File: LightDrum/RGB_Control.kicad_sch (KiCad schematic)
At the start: 0 parts

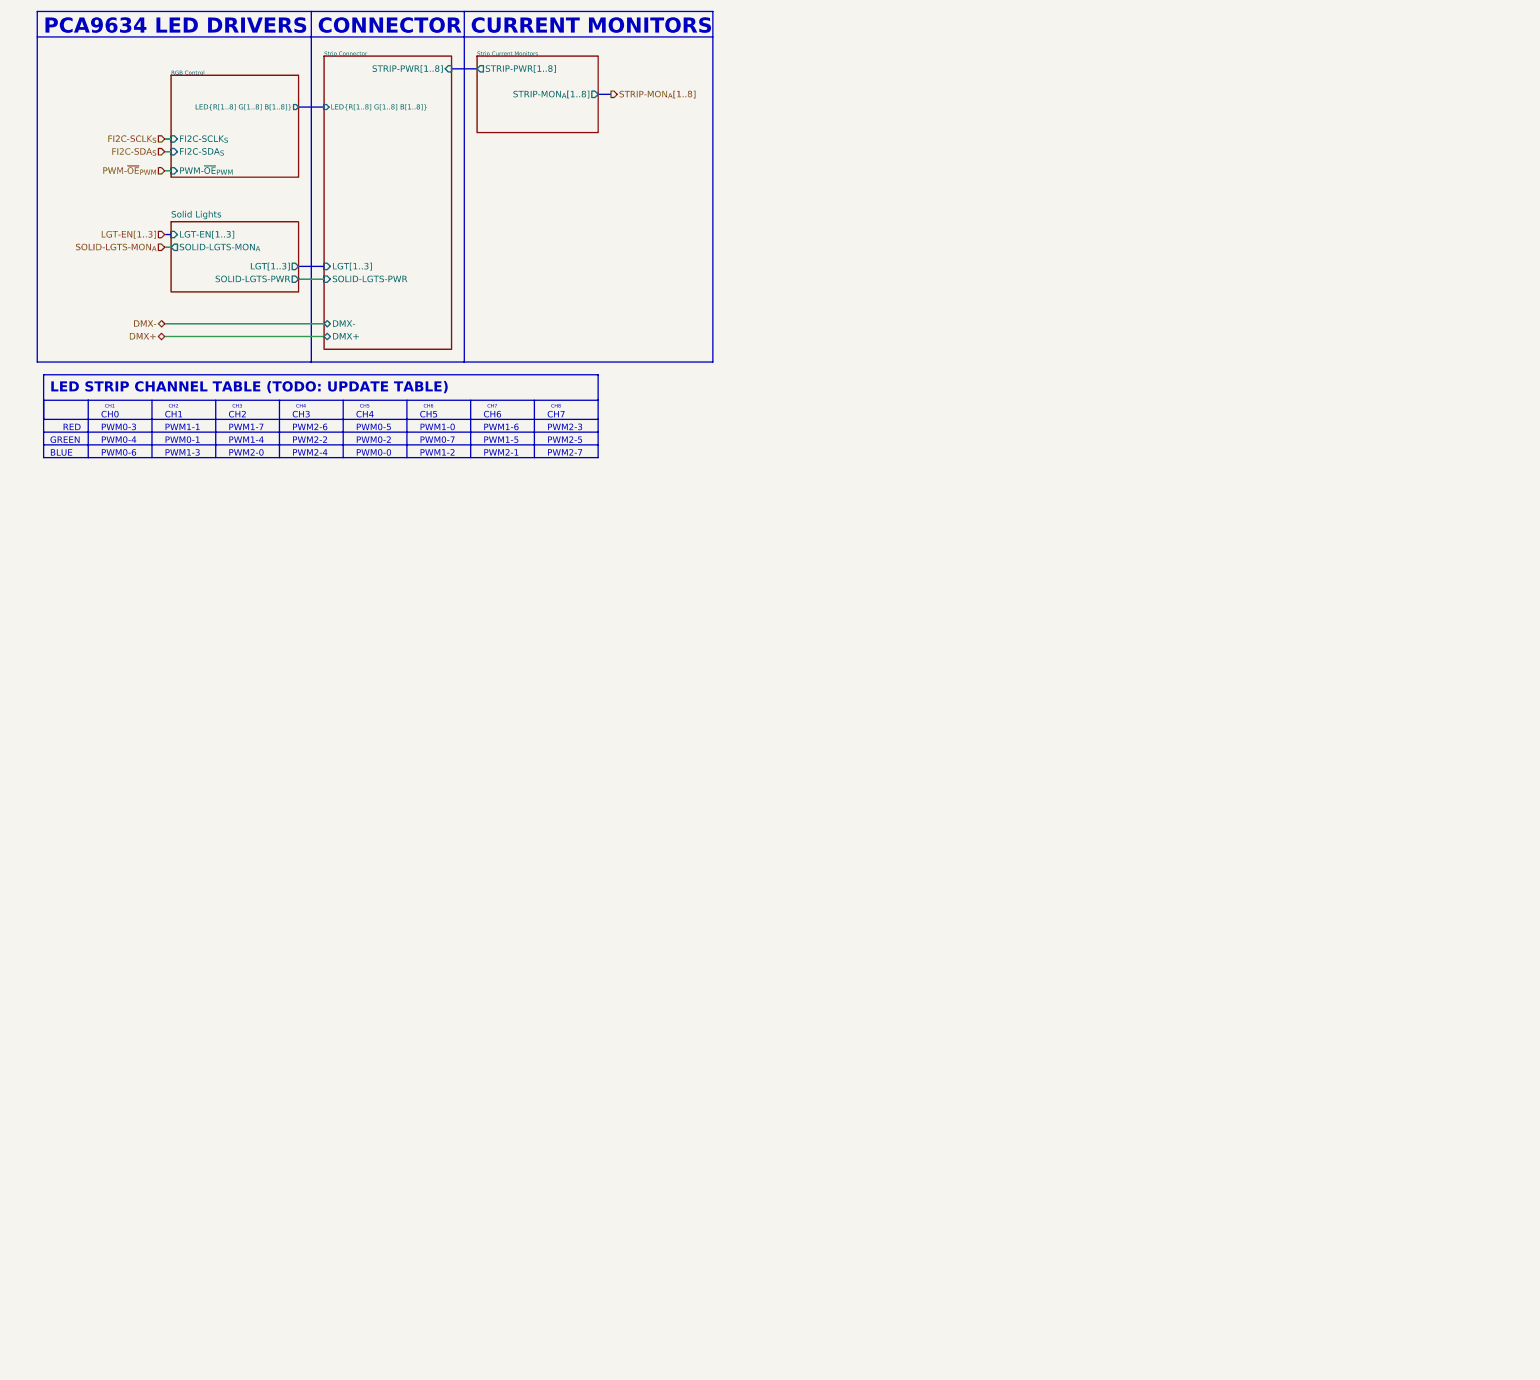
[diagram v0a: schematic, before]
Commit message: Fix schematic layout
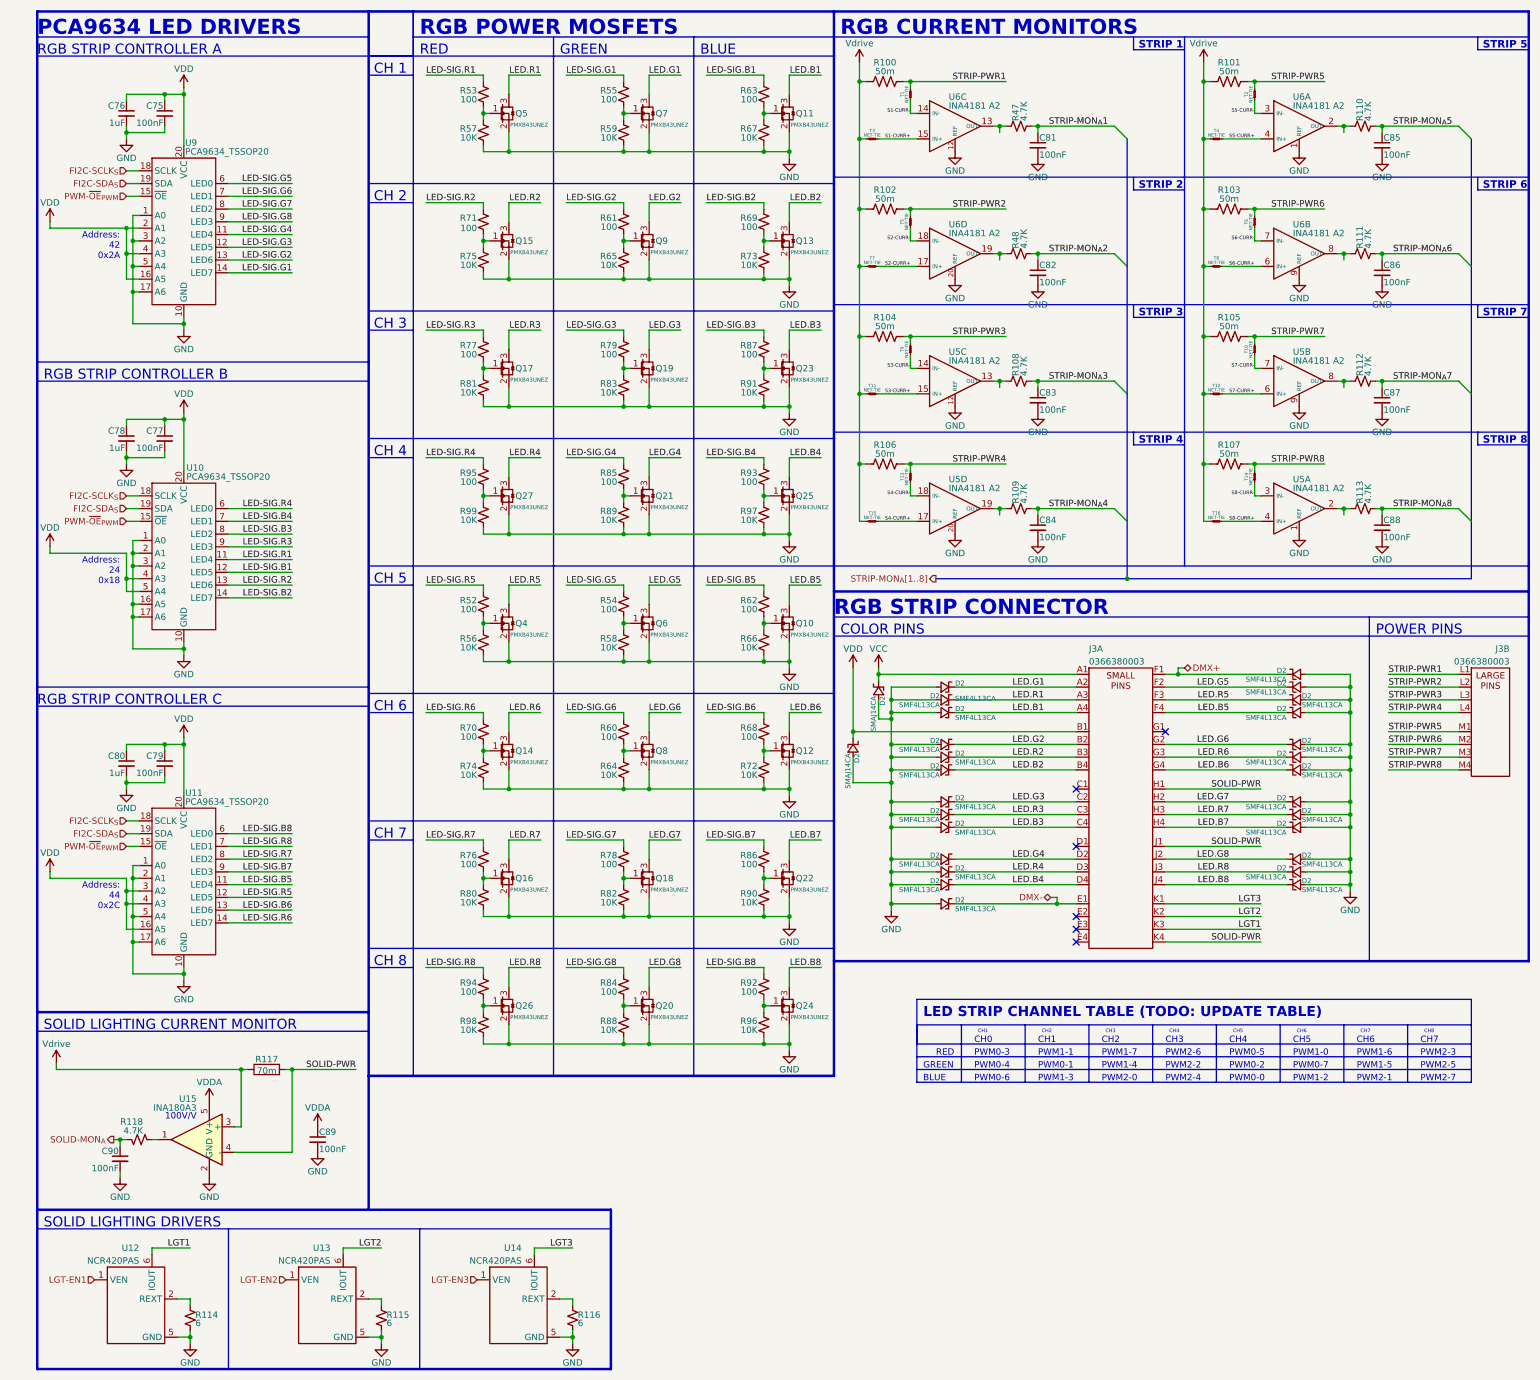
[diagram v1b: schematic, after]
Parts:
- added C75, C77, C79, C81, C82, C83, C84, C85, C86, C87, C88, C89, C90: 100nF, Capacitor_SMD:C_0402_1005Metric, symbol Daxxn_Device:C
- added C76, C78, C80: 1uF, Capacitor_SMD:C_0603_1608Metric, symbol Daxxn_Device:C
- added D2 (x26): SMF4L13CA, Diode_SMD:D_SOD-123F, symbol Daxxn_Device:D_TVS_U
- added D2 (x2): SMAJ14CA, Diode_SMD:D_SMA, symbol Daxxn_Device:D_TVS_U
- added J3: 0366380003, Daxxn_Connectors:0366380003, symbol Daxxn_Connectors:0366380003
- added Q10, Q11, Q12, Q13, Q14, Q15, Q16, Q17, Q18, Q19, Q20, Q21, Q22, Q23, Q24, Q25, Q26, Q27, Q4, Q5, Q6, Q7, Q8, Q9: PMXB43UNEZ, Daxxn_Packages:DFN1010D-3, symbol Daxxn_Transistors:PMXB43UNEZ
- added R100, R101, R102, R103, R104, R105, R106, R107: 50m, Resistor_SMD:R_2010_5025Metric, symbol Device:R_US
- added R108, R109, R110, R111, R112, R113, R118, R47, R48: 4.7K, Resistor_SMD:R_0402_1005Metric, symbol Daxxn_Device:R
- added R114, R115, R116: 6, Resistor_SMD:R_0402_1005Metric, symbol Daxxn_Device:R
- added R117: 70m, Resistor_SMD:R_1206_3216Metric, symbol Daxxn_Device:R_Shunt
- added R52, R53, R54, R55, R60, R61, R62, R63, R68, R69, R70, R71, R76, R77, R78, R79, R84, R85, R86, R87, R92, R93, R94, R95: 100, Resistor_SMD:R_0402_1005Metric, symbol Device:R_Small_US
- added R56, R57, R58, R59, R64, R65, R66, R67, R72, R73, R74, R75, R80, R81, R82, R83, R88, R89, R90, R91, R96, R97, R98, R99: 10K, Resistor_SMD:R_0402_1005Metric, symbol Device:R_Small_US
- added T1, T10, T11, T12, T13, T14, T15, T16, T2, T3, T4, T5, T6, T7, T8, T9: NET-TIE, Daxxn_Other:NetTie-2-SMALL_SMD_Pad0.2mm, symbol Daxxn_Other:NET-TIE
- added U10, U11, U9: PCA9634_TSSOP20, Daxxn_Packages:TSSOP-20_4.4x6.5mm_P0.65mm, symbol Daxxn_IC:PCA9634_TSSOP20
- added U12, U13, U14: NCR420PAS, Daxxn_Packages:DFN2020D-6_2x2mm-P0.65mm, symbol Daxxn_IC:NCR420PAS
- added U15: INA180A3, Package_TO_SOT_SMD:SOT-23-5, symbol Amplifier_Current:INA180A3
- added U5, U6: INA4181 A2, Package_SO:TSSOP-20_4.4x6.5mm_P0.65mm, symbol Daxxn_IC:INA4181
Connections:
- net DMX+: now also D2.1 (K), J3.F1
- net DMX-: now also D2.1 (K), J3.E1
- net FI2C-SCLK_{S}: now also U10.18 (SCLK), U11.18 (SCLK), U9.18 (SCLK)
- net FI2C-SDA_{S}: now also U10.19 (SDA), U11.19 (SDA), U9.19 (SDA)
- net PWM-~{OE}_{PWM}: now also U10.15 (~{OE}), U11.15 (~{OE}), U9.15 (~{OE})
- new net: Q5.1 (G), R53.2, R57.1
- new net: Q26.1 (G), R94.2, R98.1
- new net: Q25.1 (G), R93.2, R97.1
- new net: R114.1, U12.2 (REXT)
- new net: U12.3 (NC), U12.4 (NC), U12.8 (NC)
- new net: R110.1, U6.2 (OUT)
- new net: Q11.1 (G), R63.2, R67.1
- new net: Q23.1 (G), R87.2, R91.1
- new net: R47.1, U6.13 (OUT)
- new net: Q22.1 (G), R86.2, R90.1
- new net: Q9.1 (G), R61.2, R65.1
- new net: Q13.1 (G), R69.2, R73.1
- new net: Q15.1 (G), R71.2, R75.1
- new net: Q16.1 (G), R76.2, R80.1
- new net: R109.1, U5.19 (OUT)
- new net: R118.1, U15.1
- new net: Q8.1 (G), R60.2, R64.1
- new net: R116.1, U14.2 (REXT)
- new net: R112.1, U5.8 (OUT)
- new net: Q10.1 (G), R62.2, R66.1
- new net: R111.1, U6.8 (OUT)
- new net: Q17.1 (G), R77.2, R81.1
- new net: Q19.1 (G), R79.2, R83.1
- new net: R108.1, U5.13 (OUT)
- new net: Q14.1 (G), R70.2, R74.1
- new net: Q12.1 (G), R68.2, R72.1
- new net: Q24.1 (G), R92.2, R96.1
- new net: Q6.1 (G), R54.2, R58.1
- new net: Q27.1 (G), R95.2, R99.1
- new net: Q7.1 (G), R55.2, R59.1
- new net: Q4.1 (G), R52.2, R56.1
- new net: Q21.1 (G), R85.2, R89.1
- new net: Q20.1 (G), R84.2, R88.1
- new net: U14.3 (NC), U14.4 (NC), U14.8 (NC)
- new net: R113.1, U5.2 (OUT)
- new net: R115.1, U13.2 (REXT)
- new net: U13.3 (NC), U13.4 (NC), U13.8 (NC)
- new net: Q18.1 (G), R78.2, R82.1
- new net: R48.1, U6.19 (OUT)
- new net GND: C75.2, C76.2, C77.2, C78.2, C79.2, C80.2, C81.2, C82.2, C83.2, C84.2, C85.2, C86.2, C87.2, C88.2, C89.2, C90.2, D2.2 (A), D2.2 (A), D2.2 (A), D2.2 (A), D2.2 (A), D2.2 (A), D2.2 (A), D2.2 (A), D2.2 (A), D2.2 (A), D2.2 (A), D2.2 (A), D2.2 (A), D2.2 (A), D2.2 (A), D2.2 (A), D2.2 (A), D2.2 (A), D2.2 (A), D2.2 (A), D2.2 (A), D2.2 (A), D2.2 (A), D2.2 (A), D2.2 (A), D2.2 (A), D2.2 (A), D2.2 (A), Q10.2 (S), Q11.2 (S), Q12.2 (S), Q13.2 (S), Q14.2 (S), Q15.2 (S), Q16.2 (S), Q17.2 (S), Q18.2 (S), Q19.2 (S), Q20.2 (S), Q21.2 (S), Q22.2 (S), Q23.2 (S), Q24.2 (S), Q25.2 (S), Q26.2 (S), Q27.2 (S), Q4.2 (S), Q5.2 (S), Q6.2 (S), Q7.2 (S), Q8.2 (S), Q9.2 (S), R114.2, R115.2, R116.2, R56.2, R57.2, R58.2, R59.2, R64.2, R65.2, R66.2, R67.2, R72.2, R73.2, R74.2, R75.2, R80.2, R81.2, R82.2, R83.2, R88.2, R89.2, R90.2, R91.2, R96.2, R97.2, R98.2, R99.2, U10.1 (A0), U10.10 (GND), U10.16 (A5), U10.17 (A6), U10.2 (A1), U10.3 (A2), U11.1 (A0), U11.10 (GND), U11.17 (A6), U11.2 (A1), U11.5 (A4), U12.5 (GND), U13.5 (GND), U14.5 (GND), U15.2 (GND), U5.1 (REF), U5.12 (REF), U5.20 (REF), U5.9 (REF), U6.1 (REF), U6.12 (REF), U6.20 (REF), U6.9 (REF), U9.1 (A0), U9.10 (GND), U9.17 (A6), U9.3 (A2), U9.5 (A4)
- new net LED-SIG.B1: R63.1, U10.12 (LED5)
- new net LED-SIG.B2: R69.1, U10.14 (LED7)
- new net LED-SIG.B3: R87.1, U10.8 (LED2)
- new net LED-SIG.B4: R93.1, U10.7 (LED1)
- new net LED-SIG.B5: R62.1, U11.11 (LED4)
- new net LED-SIG.B6: R68.1, U11.13 (LED6)
- new net LED-SIG.B7: R86.1, U11.9 (LED3)
- new net LED-SIG.B8: R92.1, U11.6 (LED0)
- new net LED-SIG.G1: R55.1, U9.14 (LED7)
- new net LED-SIG.G2: R61.1, U9.13 (LED6)
- new net LED-SIG.G3: R79.1, U9.12 (LED5)
- new net LED-SIG.G4: R85.1, U9.11 (LED4)
- new net LED-SIG.G5: R54.1, U9.6 (LED0)
- new net LED-SIG.G6: R60.1, U9.7 (LED1)
- new net LED-SIG.G7: R78.1, U9.8 (LED2)
- new net LED-SIG.G8: R84.1, U9.9 (LED3)
- new net LED-SIG.R1: R53.1, U10.11 (LED4)
- new net LED-SIG.R2: R71.1, U10.13 (LED6)
- new net LED-SIG.R3: R77.1, U10.9 (LED3)
- new net LED-SIG.R4: R95.1, U10.6 (LED0)
- new net LED-SIG.R5: R52.1, U11.12 (LED5)
- new net LED-SIG.R6: R70.1, U11.14 (LED7)
- new net LED-SIG.R7: R76.1, U11.8 (LED2)
- new net LED-SIG.R8: R94.1, U11.7 (LED1)
- new net LED.B1: D2.1 (K), J3.A4, Q11.3 (D)
- new net LED.B2: D2.1 (K), J3.B4, Q13.3 (D)
- new net LED.B3: D2.1 (K), J3.C4, Q23.3 (D)
- new net LED.B4: D2.1 (K), J3.D4, Q25.3 (D)
- new net LED.B5: D2.1 (K), J3.F4, Q10.3 (D)
- new net LED.B6: D2.1 (K), J3.G4, Q12.3 (D)
- new net LED.B7: D2.1 (K), J3.H4, Q22.3 (D)
- new net LED.B8: D2.1 (K), J3.J4, Q24.3 (D)
- new net LED.G1: D2.1 (K), J3.A2, Q7.3 (D)
- new net LED.G2: D2.1 (K), J3.B2, Q9.3 (D)
- new net LED.G3: D2.1 (K), J3.C2, Q19.3 (D)
- new net LED.G4: D2.1 (K), J3.D2, Q21.3 (D)
- new net LED.G5: D2.1 (K), J3.F2, Q6.3 (D)
- new net LED.G6: D2.1 (K), J3.G2, Q8.3 (D)
- new net LED.G7: D2.1 (K), J3.H2, Q18.3 (D)
- new net LED.G8: D2.1 (K), J3.J2, Q20.3 (D)
- new net LED.R1: D2.1 (K), J3.A3, Q5.3 (D)
- new net LED.R2: D2.1 (K), J3.B3, Q15.3 (D)
- new net LED.R3: D2.1 (K), J3.C3, Q17.3 (D)
- new net LED.R4: D2.1 (K), J3.D3, Q27.3 (D)
- new net LED.R5: D2.1 (K), J3.F3, Q4.3 (D)
- new net LED.R6: D2.1 (K), J3.G3, Q14.3 (D)
- new net LED.R7: D2.1 (K), J3.H3, Q16.3 (D)
- new net LED.R8: D2.1 (K), J3.J3, Q26.3 (D)
- new net LGT-EN1: U12.1 (VEN)
- new net LGT-EN2: U13.1 (VEN)
- new net LGT-EN3: U14.1 (VEN)
- new net LGT1: J3.K3, U12.6 (IOUT), U12.7 (IOUT)
- new net LGT2: J3.K2, U13.6 (IOUT), U13.7 (IOUT)
- new net LGT3: J3.K1, U14.6 (IOUT), U14.7 (IOUT)
- new net S1-CURR+: T3.2, U6.15 (IN+)
- new net S1-CURR-: T1.1, U6.14 (IN-)
- new net S2-CURR+: T7.2, U6.17 (IN+)
- new net S2-CURR-: T5.1, U6.18 (IN-)
- new net S3-CURR+: T11.2, U5.15 (IN+)
- new net S3-CURR-: T9.1, U5.14 (IN-)
- new net S4-CURR+: T15.2, U5.17 (IN+)
- new net S4-CURR-: T13.1, U5.18 (IN-)
- new net S5-CURR+: T4.2, U6.4 (IN+)
- new net S5-CURR-: T2.1, U6.3 (IN-)
- new net S6-CURR+: T8.2, U6.6 (IN+)
- new net S6-CURR-: T6.1, U6.7 (IN-)
- new net S7-CURR+: T12.2, U5.6 (IN+)
- new net S7-CURR-: T10.1, U5.7 (IN-)
- new net S8-CURR+: T16.2, U5.4 (IN+)
- new net S8-CURR-: T14.1, U5.3 (IN-)
- new net SOLID-MON_{A}: C90.1, R118.2
- new net SOLID-PWR: J3.H1, J3.J1, J3.K4, R117.2, U15.4 (-)
- new net STRIP-MON_{A}1: C81.1, R47.2
- new net STRIP-MON_{A}2: C82.1, R48.2
- new net STRIP-MON_{A}3: C83.1, R108.2
- new net STRIP-MON_{A}4: C84.1, R109.2
- new net STRIP-MON_{A}5: C85.1, R110.2
- new net STRIP-MON_{A}6: C86.1, R111.2
- new net STRIP-MON_{A}7: C87.1, R112.2
- new net STRIP-MON_{A}8: C88.1, R113.2
- new net STRIP-PWR1: J3.L1, R100.2, T1.2
- new net STRIP-PWR2: J3.L2, R102.2, T5.2
- new net STRIP-PWR3: J3.L3, R104.2, T9.2
- new net STRIP-PWR4: J3.L4, R106.2, T13.2
- new net STRIP-PWR5: J3.M1, R101.2, T2.2
- new net STRIP-PWR6: J3.M2, R103.2, T6.2
- new net STRIP-PWR7: J3.M3, R105.2, T10.2
- new net STRIP-PWR8: J3.M4, R107.2, T14.2
- new net VCC: D2.1 (K), J3.A1
- new net VDD: C75.1, C76.1, C77.1, C78.1, C79.1, C80.1, D2.1 (K), J3.B1, U10.20 (VCC), U10.4 (A3), U10.5 (A4), U11.16 (A5), U11.20 (VCC), U11.3 (A2), U11.4 (A3), U9.16 (A5), U9.2 (A1), U9.20 (VCC), U9.4 (A3)
- new net VDDA: C89.1, U15.5 (V+)
- new net Vdrive: R100.1, R101.1, R102.1, R103.1, R104.1, R105.1, R106.1, R107.1, R117.1, T11.1, T12.1, T15.1, T16.1, T3.1, T4.1, T7.1, T8.1, U15.3 (+)
- no-connect marks 0 -> 6
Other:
- removed sheet RGB Control
- removed sheet Solid Lights
- removed sheet Strip Connector
- removed sheet Strip Current Monitors
- note added: "100V/V"
- note added: "Address: 24 0x18"
- note added: "Address: 42 0x2A"
- note added: "Address: 44 0x2C"
- note added: "CH 1"
- note added: "CH 2"
- note added: "CH 3"
- note added: "CH 4"
- note added: "CH 5"
- note added: "CH 6"
- note added: "CH 7"
- note added: "CH 8"
- note added: "COLOR PINS"
- note added: "POWER PINS"
- note added: "RGB CURRENT MONITORS"
- note added: "RGB POWER MOSFETS"
- note added: "RGB STRIP CONNECTOR"
- note added: "RGB STRIP CONTROLLER A"
- note added: "RGB STRIP CONTROLLER B"
- note added: "RGB STRIP CONTROLLER C"
- note added: "SOLID LIGHTING CURRENT MONITOR"
- note added: "SOLID LIGHTING DRIVERS"
- note added: "STRIP 1"
- note added: "STRIP 2"
- note added: "STRIP 3"
- note added: "STRIP 4"
- note added: "STRIP 5"
- note added: "STRIP 6"
- note added: "STRIP 7"
- note added: "STRIP 8"
- note removed: "CONNECTOR"
- note removed: "CURRENT MONITORS"
